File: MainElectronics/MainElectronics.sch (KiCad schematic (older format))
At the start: 35 parts, among them J1 NVIDIA_Jetson_NX_Dev_40pin_Co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, J2 NVIDIA_Jetson_NX_Dev_Button_C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, J3 Jetson_DC_In, M1 Motor_DC, M2 Motor_DC, M3 Motor_DC, M4 Motor_DC, M5 Motor_DC, M6 Motor_DC, M7 Motor_DC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

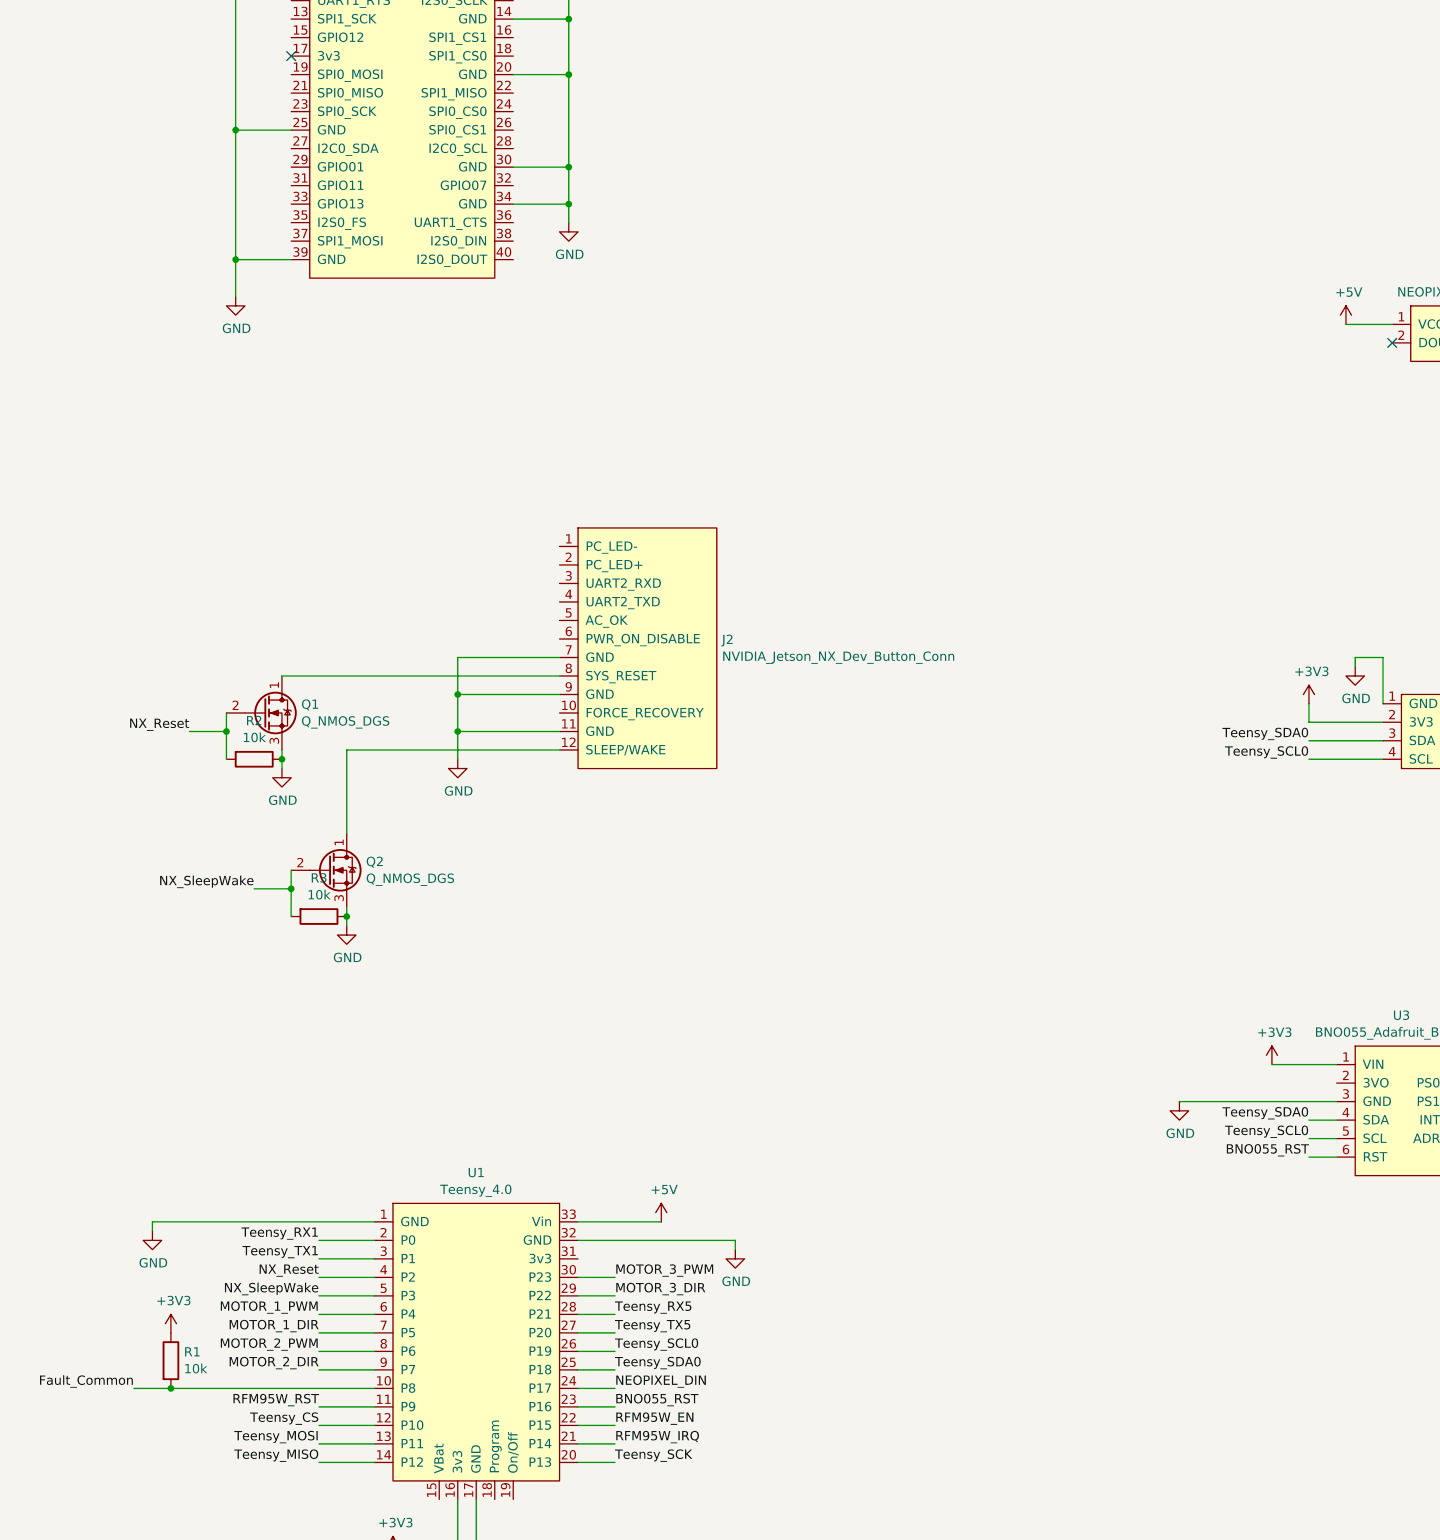
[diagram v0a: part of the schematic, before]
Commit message: Swapped BNO055 to Jetson
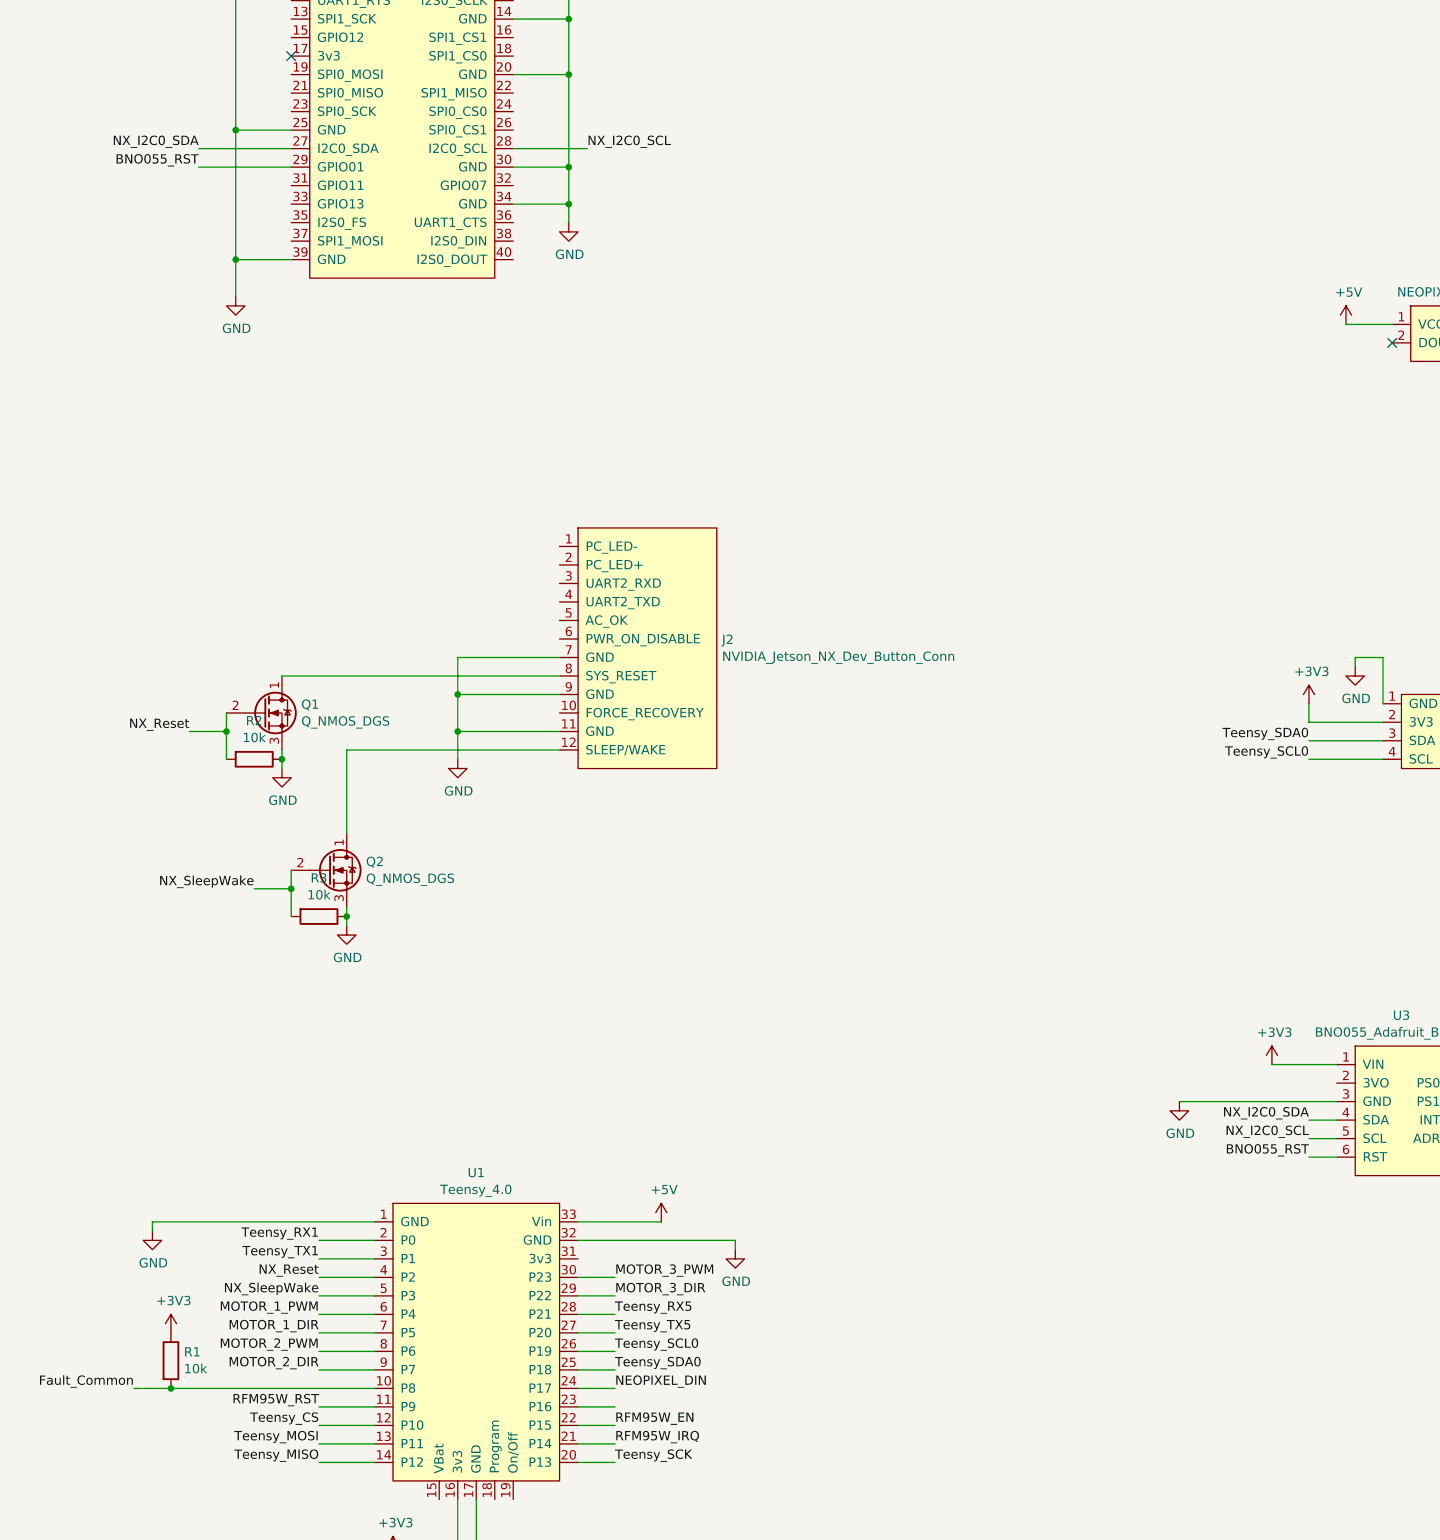
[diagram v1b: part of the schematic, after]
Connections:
- net BNO055_RST: now also J1.29 (GPIO01); no longer U1.23 (P16)
- net Teensy_SCL0: no longer U3.5 (SCL)
- net Teensy_SDA0: no longer U3.4 (SDA)
- net NX_I2C0_SDA: now reaches J1.27 (I2C0_SDA)
- net NX_I2C0_SDA: now also U3.4 (SDA)
- net NX_I2C0_SCL: now reaches J1.28 (I2C0_SCL)
- net NX_I2C0_SCL: now also U3.5 (SCL)
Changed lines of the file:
@@
 Text Label 7650 6450 2    50   ~ 0
 Teensy_SDA0
-Text Label 7650 8600 2    50   ~ 0
-Teensy_SCL0
 Wire Wire Line
 	7650 8600 7800 8600
-Text Label 7650 8500 2    50   ~ 0
-Teensy_SDA0
 Wire Wire Line
 	7650 8500 7800 8500
@@
 Wire Wire Line
 	7650 8700 7800 8700
-Text Label 3900 10050 0    50   ~ 0
-BNO055_RST
 Wire Wire Line
 	3900 10050 3700 10050
@@
 Wire Wire Line
 	3350 2350 4000 2350
+Text Label 1650 3250 2    50   ~ 0
+NX_I2C0_SDA
+Text Label 3750 3250 0    50   ~ 0
+NX_I2C0_SCL
+Wire Wire Line
+	3750 3250 3350 3250
+Wire Wire Line
+	2150 3250 1650 3250
+Text Label 7650 8600 2    50   ~ 0
+NX_I2C0_SCL
+Text Label 7650 8500 2    50   ~ 0
+NX_I2C0_SDA
+Text Label 1650 3350 2    50   ~ 0
+BNO055_RST
+Wire Wire Line
+	1650 3350 2150 3350
 $EndSCHEMATC

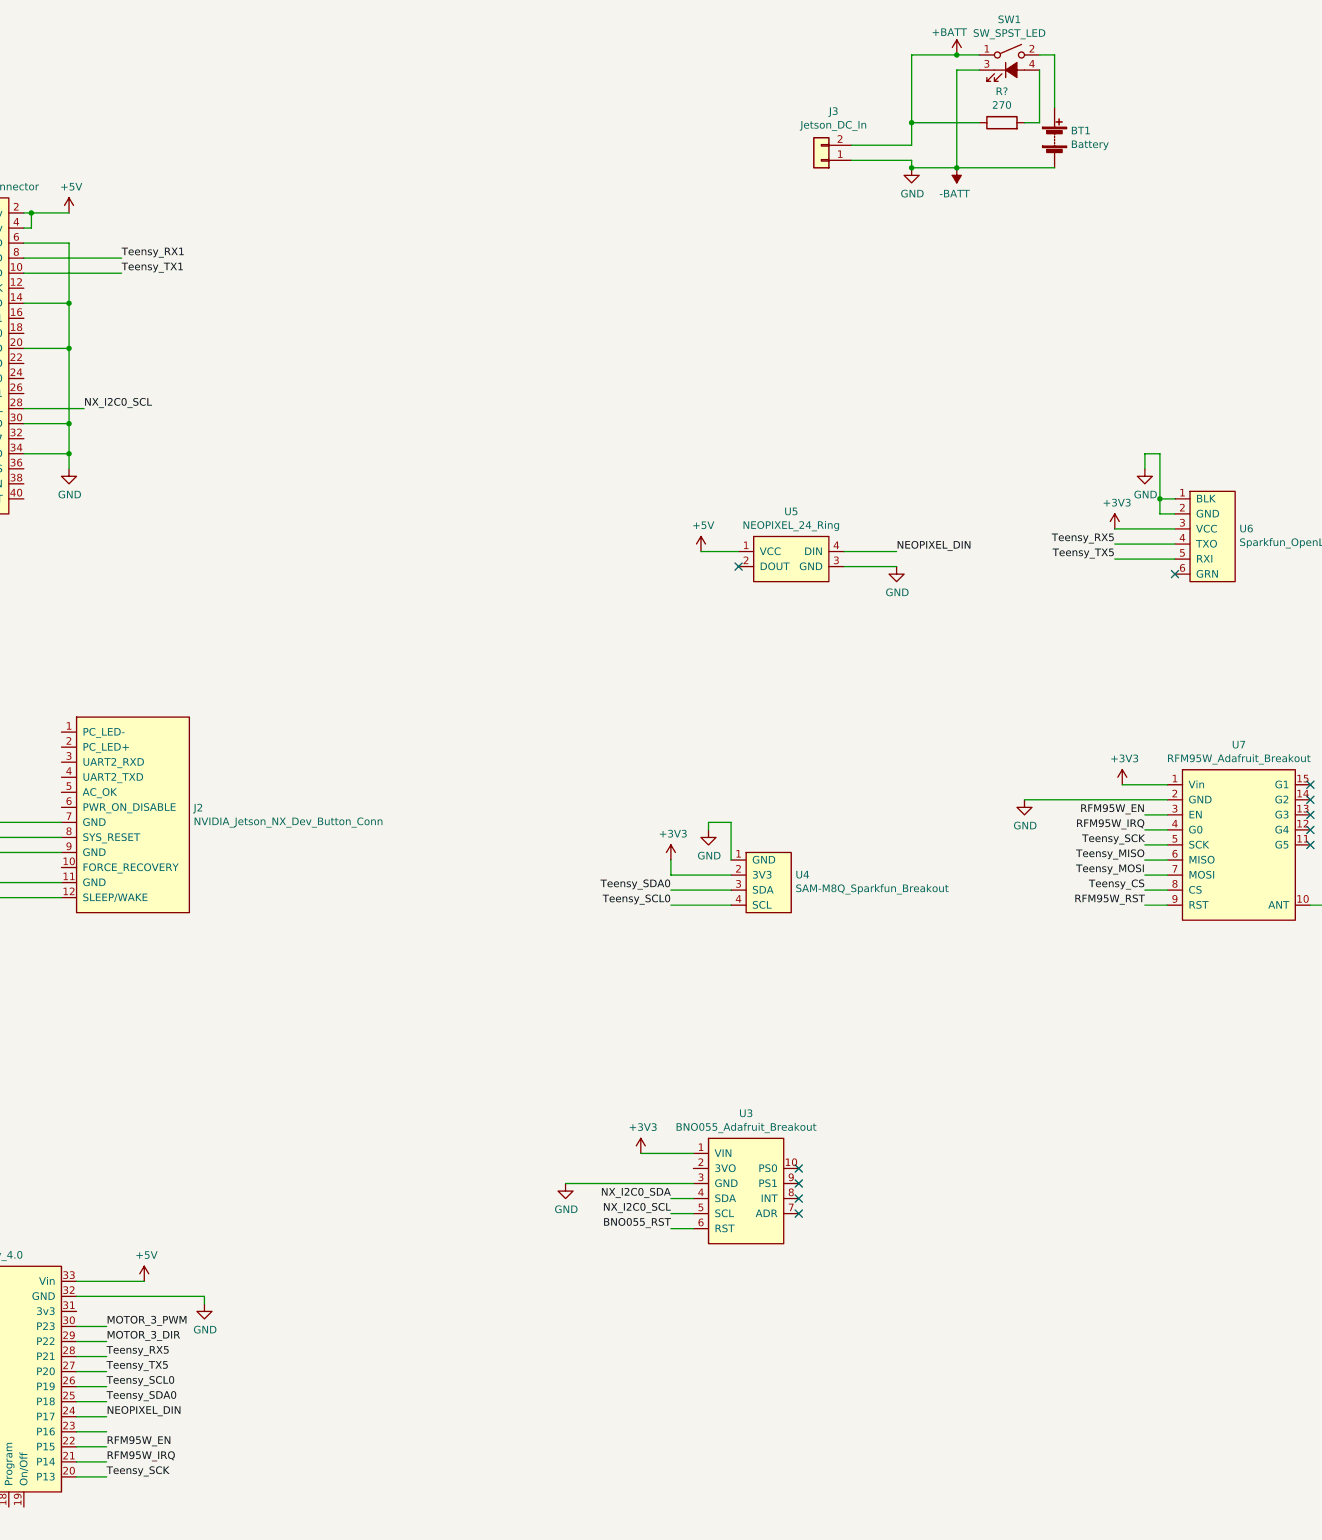
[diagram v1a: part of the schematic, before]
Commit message: Probably should only kill motors with e-stop
Also voltage sense with freed up teensy pin
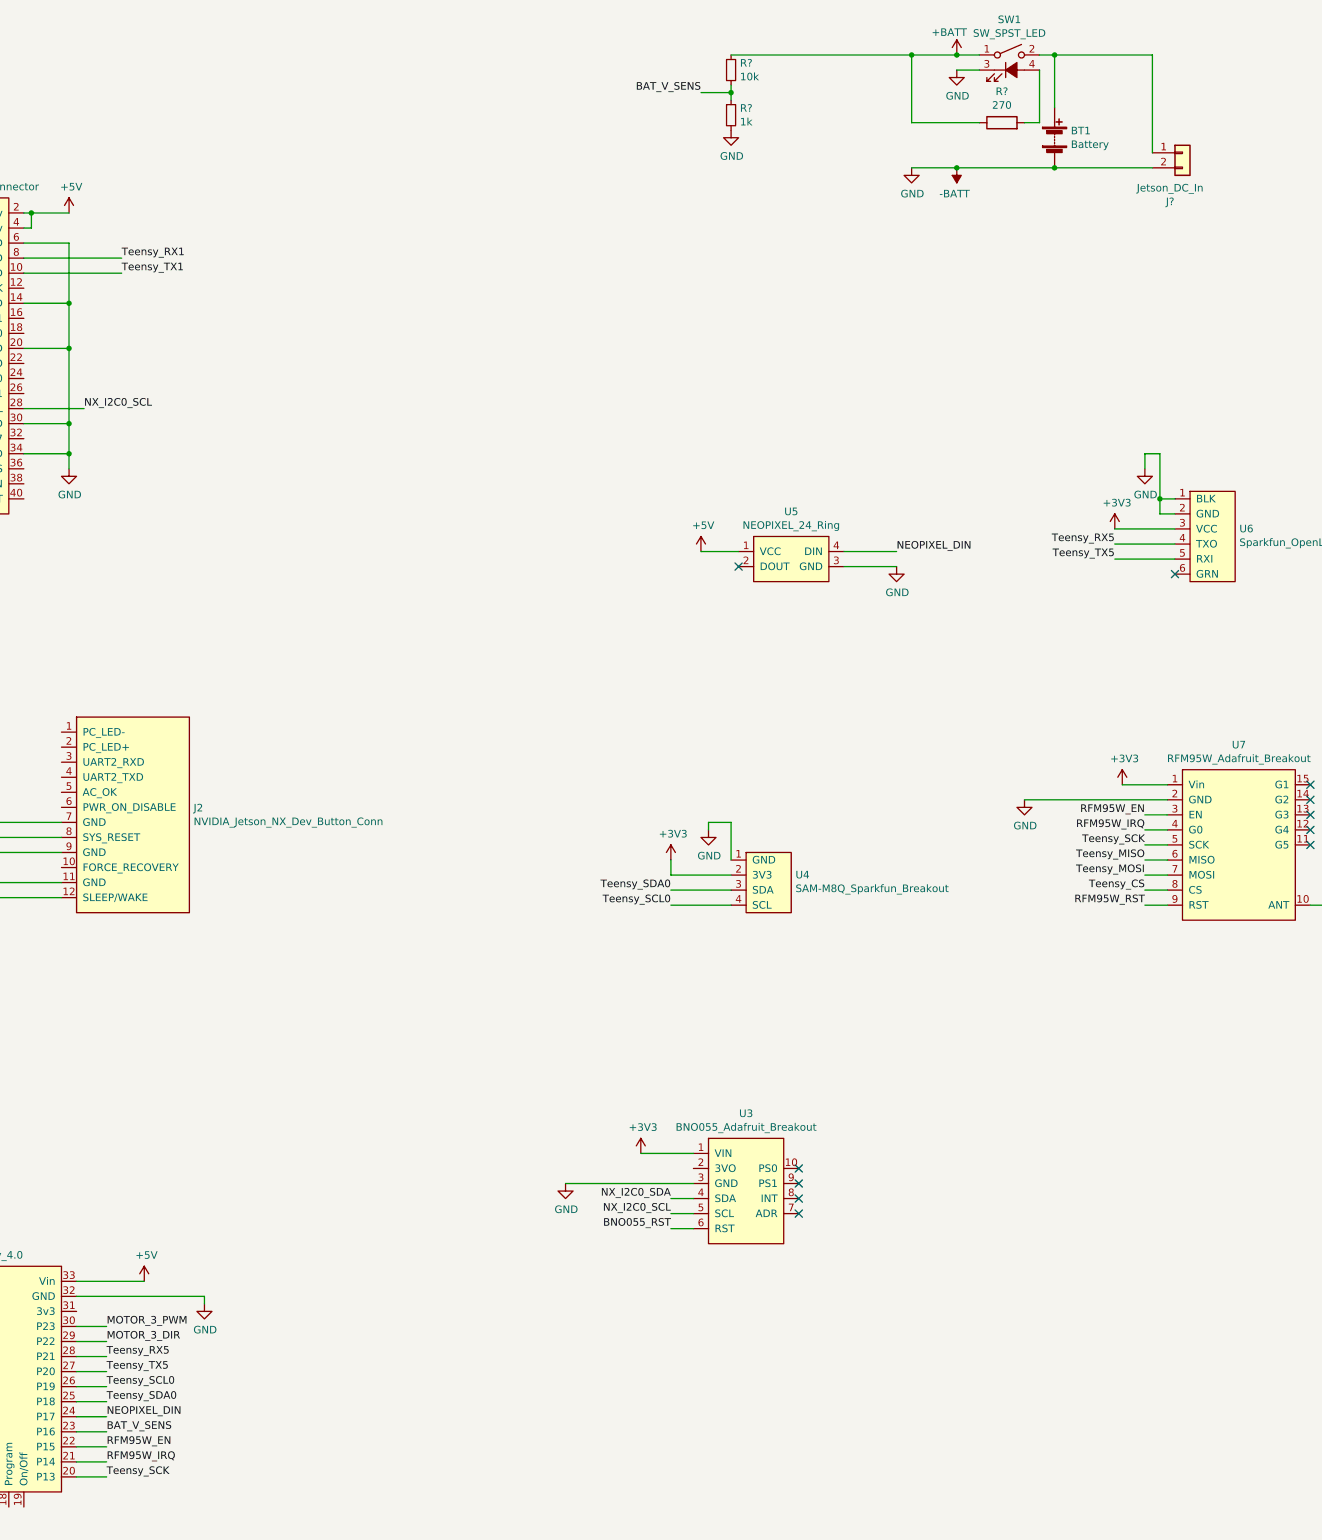
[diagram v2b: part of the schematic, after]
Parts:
- removed J3: Jetson_DC_In, symbol Connector_Generic:Conn_01x02
- added J?: Jetson_DC_In, symbol Connector_Generic:Conn_01x02
- added R?: 10k, symbol Device:R_Small
- added R?: 1k, symbol Device:R_Small
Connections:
- net +BATT: now also R?.1
- net -BATT: now also J?.2 (Pin_2), R?.2
- net at BT1.1 (+), SW1.2: now also J?.1 (Pin_1)
- net BAT_V_SENS: now reaches U1.23 (P16)
- net BAT_V_SENS: now also R?.1, R?.2
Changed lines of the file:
@@
 	1    0    0    -1
 $EndComp
-$Comp
-L Connector_Generic:Conn_01x02 J3
-U 1 1 5EDED200
-P 8650 1600
-F 0 "J3" H 8568 1275 50  0000 C CNN
-F 1 "Jetson_DC_In" H 8568 1366 50  0000 C CNN
-F 2 "" H 8650 1600 50  0001 C CNN
-F 3 "~" H 8650 1600 50  0001 C CNN
-	1    8650 1600
-	-1   0    0    1
-$EndComp
-Wire Wire Line
-	9250 1500 8850 1500
-Wire Wire Line
-	8850 1600 9250 1600
-Wire Wire Line
-	9250 1600 9250 1650
-Wire Wire Line
-	9250 1650 9550 1650
 Wire Wire Line
 	9550 900  9250 900
@@
 	9700 900  9550 900
 Connection ~ 9550 900
-Wire Wire Line
-	10200 1650 9550 1650
-Connection ~ 9550 1650
 $Comp
 L power:+5V #PWR09
@@
 	1    0    0    -1
 $EndComp
-Connection ~ 9250 1650
 NoConn ~ 15850 1750
 NoConn ~ 15150 2050
@@
 	9700 1000 9550 1000
 Wire Wire Line
-	9550 1000 9550 1650
-Wire Wire Line
 	9250 900  9250 1350
 $Comp
@@
 Wire Wire Line
 	9700 1350 9250 1350
-Connection ~ 9250 1350
-Wire Wire Line
-	9250 1350 9250 1500
 Wire Wire Line
 	3350 2250 4000 2250
@@
 Wire Wire Line
 	1650 3350 2150 3350
+Text Label 3900 10050 0    50   ~ 0
+BAT_V_SENS
+Text Label 7850 1150 2    50   ~ 0
+BAT_V_SENS
+$Comp
+L Device:R_Small R?
+U 1 1 5FA0E42F
+P 8050 1000
+F 0 "R?" H 8109 1046 50  0000 L CNN
+F 1 "10k" H 8109 955 50  0000 L CNN
+F 2 "" H 8050 1000 50  0001 C CNN
+F 3 "~" H 8050 1000 50  0001 C CNN
+	1    8050 1000
+	1    0    0    -1
+$EndComp
+$Comp
+L Device:R_Small R?
+U 1 1 5FA0ED9A
+P 8050 1300
+F 0 "R?" H 8109 1346 50  0000 L CNN
+F 1 "1k" H 8109 1255 50  0000 L CNN
+F 2 "" H 8050 1300 50  0001 C CNN
+F 3 "~" H 8050 1300 50  0001 C CNN
+	1    8050 1300
+	1    0    0    -1
+$EndComp
+Wire Wire Line
+	7850 1150 8050 1150
+Wire Wire Line
+	8050 1150 8050 1200
+Wire Wire Line
+	8050 1150 8050 1100
+Connection ~ 8050 1150
+Connection ~ 9250 900
+Wire Wire Line
+	8050 900  9250 900
+$Comp
+L power:GND #PWR?
+U 1 1 5FA6E22C
+P 8050 1400
+F 0 "#PWR?" H 8050 1150 50  0001 C CNN
+F 1 "GND" H 8055 1227 50  0000 C CNN
+F 2 "" H 8050 1400 50  0001 C CNN
+F 3 "" H 8050 1400 50  0001 C CNN
+	1    8050 1400
+	1    0    0    -1
+$EndComp
+$Comp
+L Connector_Generic:Conn_01x02 J?
+U 1 1 5FA6FEF4
+P 11050 1550
+F 0 "J?" H 10968 1225 50  0000 C CNN
+F 1 "Jetson_DC_In" H 10968 1316 50  0000 C CNN
+F 2 "" H 11050 1550 50  0001 C CNN
+F 3 "~" H 11050 1550 50  0001 C CNN
+	1    11050 1550
+	1    0    0    -1
+$EndComp
+Wire Wire Line
+	10850 1550 10850 900
+Wire Wire Line
+	10850 900  10200 900
+Connection ~ 10200 900
+Wire Wire Line
+	10200 1650 10850 1650
+Connection ~ 10200 1650
+Wire Wire Line
+	9250 1650 9550 1650
+Connection ~ 9550 1650
+Wire Wire Line
+	9550 1650 10200 1650
+$Comp
+L power:GND #PWR?
+U 1 1 5FAAB195
+P 9550 1000
+F 0 "#PWR?" H 9550 750 50  0001 C CNN
+F 1 "GND" H 9555 827 50  0000 C CNN
+F 2 "" H 9550 1000 50  0001 C CNN
+F 3 "" H 9550 1000 50  0001 C CNN
+	1    9550 1000
+	1    0    0    -1
+$EndComp
 $EndSCHEMATC
